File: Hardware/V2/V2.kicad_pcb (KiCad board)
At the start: 2 copper layers, 115 x 61 mm, 77 parts, among them J1 USB_B_Mini, Q1 MMBT2222, SW2 SW_Push, SW3 SW_Push, U1 ATmega32U4-AU, U2 LIS3DH, U4 AP2112K-3.3, Y1 16MHz

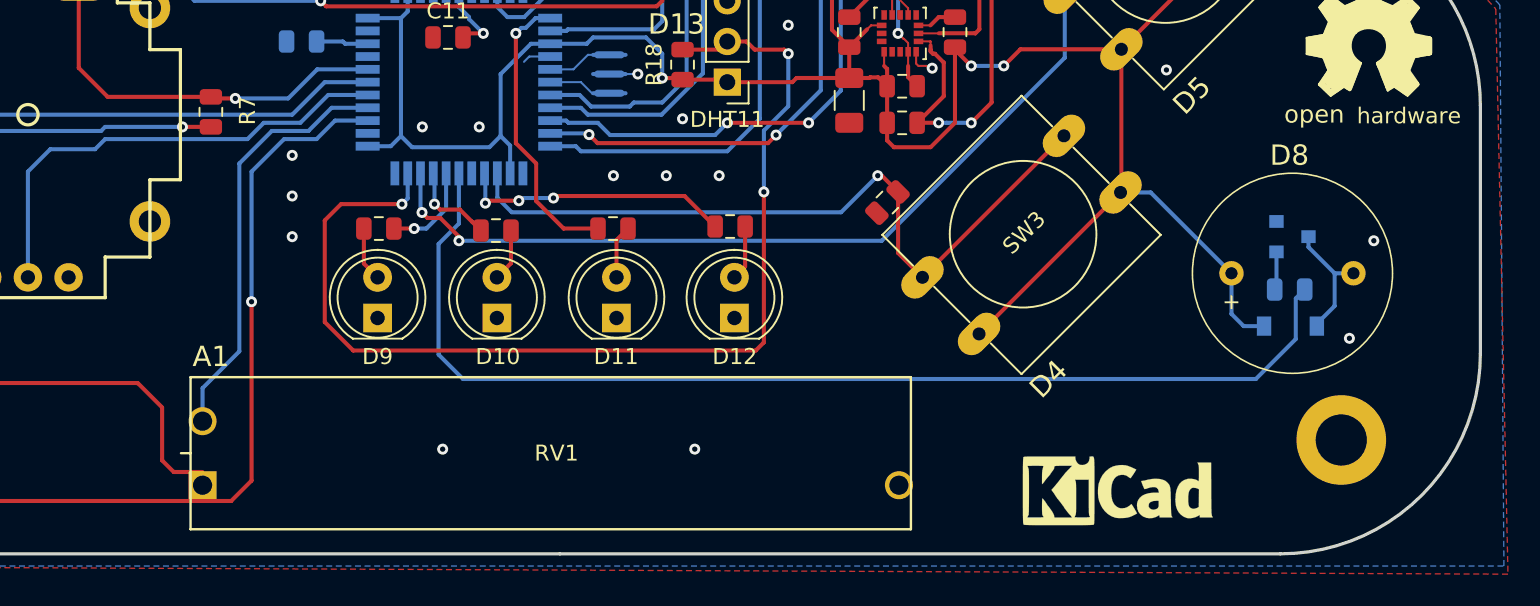
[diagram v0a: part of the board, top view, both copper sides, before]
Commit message: Serigrafias añadidas
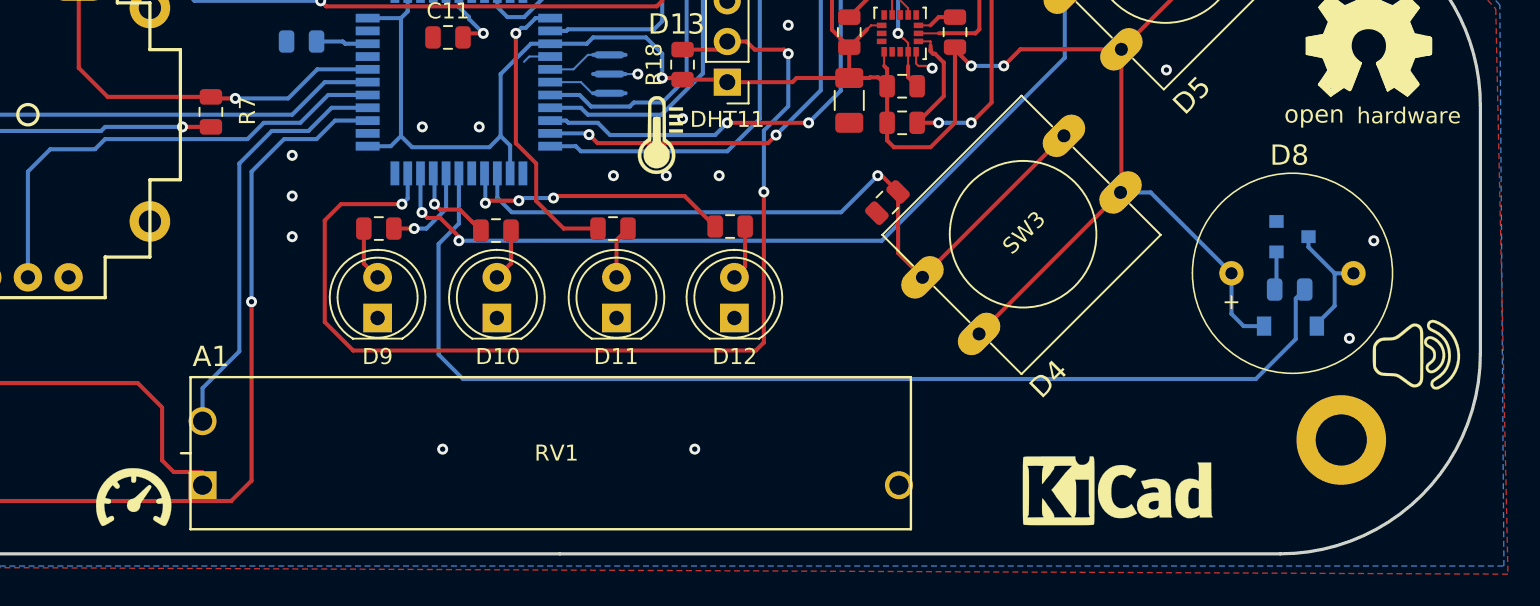
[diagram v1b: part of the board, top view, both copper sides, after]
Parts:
- added G***: LOGO, logos:altavoz, F.Cu at (209.9, 103.9)
- added G***: LOGO, logos:usb, B.Cu at (157.9, 66.9)
- added G***: LOGO, logos:bateria, B.Cu at (137.7, 61.3)
- added G***: LOGO, logos:cerebro, B.Cu at (140.1, 88.0)
- added G***: LOGO, logos:bt, B.Cu at (176.4, 76.5)
- added G***: LOGO, logos:pote, F.Cu at (129.8, 112.8)
- added G***: LOGO, logos:temp, F.Cu at (162.7, 90.2)

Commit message: DRC pasado
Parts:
- moved OLED_I2C 2.54 mm to (152.5, 71.1)
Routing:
- net GND: track 58.0 -> 60.6 mm, vias 44 -> 43
- net SDA: track 72.8 -> 74.5 mm, vias 3 -> 4
- net +3V3: track 395.9 -> 394.8 mm
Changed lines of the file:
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@@
     (thickness 1.6)
     (drawings 66)
-    (tracks 726)
+    (tracks 733)
     (zones 0)
     (modules 84)
@@
   (page A4)
   (layers
-    (0 F.Cu signal hide)
-    (31 B.Cu signal hide)
+    (0 F.Cu signal)
+    (31 B.Cu signal)
     (32 B.Adhes user)
     (33 F.Adhes user)
@@
   )
   (module Connector_PinHeader_2.54mm:PinHeader_1x04_P2.54mm_Vertical (layer F.Cu)
-    (at 152.4 73.66 90)
+    (at 152.527 71.12 90)
     (descr "Through hole straight pin header, 1x04, 2.54mm pitch, single row")
     (tags "Through hole pin header THT 1x04 2.54mm single row")
@@
   (gr_line (start 168.91 95.25) (end 142.24 95.25) (layer Dwgs.User) (width 0.127))
   (gr_line (start 168.91 67.31) (end 168.91 92.71) (layer Dwgs.User) (width 0.127))
-  (gr_line (start 142.24 67.31) (end 168.91 67.31) (layer Dwgs.User) (width 0.127))
+  (gr_line (start 142.24 69.088) (end 168.91 69.088) (layer Dwgs.User) (width 0.127))
   (segment (start 131.904 61.9) (end 133.352 60.452) (width 0.254) (layer F.Cu) (net 1))
   (segment (start 138.27 61.9) (end 138.52 61.9) (width 0.254) (layer F.Cu) (net 1) (status 30))
@@
   (segment (start 112.522 99.06) (end 120.65 99.06) (width 0.254) (layer B.Cu) (net 1) (status 20))
   (segment (start 110.998 97.536) (end 112.522 99.06) (width 0.254) (layer B.Cu) (net 1))
-  (segment (start 155.351 73.249) (end 154.94 73.66) (width 0.254) (layer F.Cu) (net 1) (status 30))
-  (segment (start 155.351 67.31) (end 155.351 73.249) (width 0.254) (layer F.Cu) (net 1) (status 30))
   (segment (start 139.954001 71.119999) (end 139.446 71.628) (width 0.254) (layer F.Cu) (net 1))
   (segment (start 139.954001 67.31) (end 139.954001 71.119999) (width 0.254) (layer F.Cu) (net 1) (status 10))
@@
   (segment (start 163.986999 86.614) (end 164.084 86.711001) (width 0.254) (layer F.Cu) (net 1) (status 30))
   (segment (start 162.814 86.614) (end 163.986999 86.614) (width 0.254) (layer F.Cu) (net 1) (status 20))
-  (segment (start 157.734 76.962) (end 157.734 77.47) (width 0.254) (layer F.Cu) (net 1) (status 30))
-  (segment (start 154.94 74.168) (end 157.734 76.962) (width 0.254) (layer F.Cu) (net 1) (status 30))
-  (segment (start 154.94 73.66) (end 154.94 74.168) (width 0.254) (layer F.Cu) (net 1) (status 30))
   (segment (start 152.02 90.932) (end 152.718 90.234) (width 0.254) (layer B.Cu) (net 1))
   (segment (start 147.192 90.932) (end 152.02 90.932) (width 0.254) (layer B.Cu) (net 1))
@@
   (segment (start 139.7 71.882) (end 139.446 71.628) (width 0.254) (layer F.Cu) (net 1))
   (segment (start 140.97 71.882) (end 139.7 71.882) (width 0.254) (layer F.Cu) (net 1))
-  (segment (start 163.068 67.056001) (end 162.814001 67.31) (width 0.254) (layer F.Cu) (net 1) (status 30))
-  (segment (start 161.38 61.9) (end 162.384 61.9) (width 0.254) (layer F.Cu) (net 1) (status 10))
-  (segment (start 163.068 65.786) (end 163.068 67.056001) (width 0.254) (layer F.Cu) (net 1) (status 20))
-  (segment (start 163.322 65.532) (end 163.068 65.786) (width 0.254) (layer F.Cu) (net 1))
-  (segment (start 162.384 61.9) (end 163.322 62.838) (width 0.254) (layer F.Cu) (net 1))
-  (segment (start 163.322 62.838) (end 163.322 65.532) (width 0.254) (layer F.Cu) (net 1))
   (segment (start 146.914 80.164) (end 146.914 81.168) (width 0.254) (layer B.Cu) (net 1) (status 20))
   (segment (start 146.812 80.062) (end 146.914 80.164) (width 0.254) (layer B.Cu) (net 1))
@@
   (segment (start 170.591 68.6735) (end 172.6565 70.739) (width 0.254) (layer F.Cu) (net 1) (status 20))
   (segment (start 170.591 67.31) (end 170.591 68.6735) (width 0.254) (layer F.Cu) (net 1) (status 10))
+  (segment (start 157.734 76.962) (end 157.734 77.47) (width 0.254) (layer F.Cu) (net 1))
+  (segment (start 155.351 74.579) (end 157.734 76.962) (width 0.254) (layer F.Cu) (net 1))
+  (segment (start 155.351 72.606081) (end 155.351 74.579) (width 0.254) (layer F.Cu) (net 1))
+  (segment (start 155.067 72.322081) (end 155.351 72.606081) (width 0.254) (layer F.Cu) (net 1))
+  (segment (start 155.067 71.12) (end 155.067 72.322081) (width 0.254) (layer F.Cu) (net 1))
+  (segment (start 154.26999 68.39101) (end 154.37001 68.39101) (width 0.254) (layer F.Cu) (net 1))
+  (segment (start 155.067 69.088) (end 155.067 71.12) (width 0.254) (layer F.Cu) (net 1))
+  (segment (start 154.37001 68.39101) (end 155.067 69.088) (width 0.254) (layer F.Cu) (net 1))
+  (segment (start 163.068 67.056001) (end 162.814001 67.31) (width 0.254) (layer F.Cu) (net 1))
+  (segment (start 163.068 65.786) (end 163.068 67.056001) (width 0.254) (layer F.Cu) (net 1))
+  (segment (start 162.941 65.659) (end 163.068 65.786) (width 0.254) (layer F.Cu) (net 1))
+  (segment (start 162.941 62.457) (end 162.941 65.659) (width 0.254) (layer F.Cu) (net 1))
+  (segment (start 162.384 61.9) (end 162.941 62.457) (width 0.254) (layer F.Cu) (net 1))
+  (segment (start 161.38 61.9) (end 162.384 61.9) (width 0.254) (layer F.Cu) (net 1))
   (segment (start 204.816 98.806) (end 205.994 98.806) (width 0.254) (layer B.Cu) (net 2) (status 20))
   (segment (start 203.184 97.174) (end 204.816 98.806) (width 0.254) (layer B.Cu) (net 2))
@@
   (segment (start 152.146 78.486) (end 152.146 79.248) (width 0.254) (layer B.Cu) (net 3))
   (segment (start 153.416 77.216) (end 152.146 78.486) (width 0.254) (layer B.Cu) (net 3) (status 10))
-  (segment (start 152.4 76.297) (end 152.4 73.66) (width 0.254) (layer B.Cu) (net 3) (status 20))
-  (segment (start 151.481 77.216) (end 152.4 76.297) (width 0.254) (layer B.Cu) (net 3) (status 10))
   (segment (start 141.964 67.31) (end 141.829001 67.31) (width 0.254) (layer F.Cu) (net 3) (status 30))
   (segment (start 143.42 65.854) (end 141.964 67.31) (width 0.254) (layer F.Cu) (net 3) (status 20))
@@
   (via (at 170.688 76.708) (size 0.6858) (drill 0.3302) (layers F.Cu B.Cu) (net 3))
   (via (at 163.83 70.866) (size 0.6858) (drill 0.3302) (layers F.Cu B.Cu) (net 3))
-  (via (at 160.02 70.866) (size 0.6858) (drill 0.3302) (layers F.Cu B.Cu) (net 3))
   (via (at 154.94 57.404) (size 0.6858) (drill 0.3302) (layers F.Cu B.Cu) (net 3))
   (via (at 156.21 57.404) (size 0.6858) (drill 0.3302) (layers F.Cu B.Cu) (net 3))
@@
   (via (at 139.7 93.98) (size 0.6858) (drill 0.3302) (layers F.Cu B.Cu) (net 3))
   (via (at 139.7 96.52) (size 0.6858) (drill 0.3302) (layers F.Cu B.Cu) (net 3))
+  (segment (start 152.527 73.533) (end 152.527 71.12) (width 0.254) (layer B.Cu) (net 3))
+  (segment (start 152.527 76.17) (end 152.527 73.533) (width 0.254) (layer B.Cu) (net 3))
+  (segment (start 151.481 77.216) (end 152.527 76.17) (width 0.254) (layer B.Cu) (net 3))
   (segment (start 149.606 78.486) (end 149.606 77.216) (width 0.254) (layer B.Cu) (net 4) (status 20))
   (segment (start 150.914 79.794) (end 149.606 78.486) (width 0.254) (layer B.Cu) (net 4))
@@
   (segment (start 178.172999 85.852) (end 178.172999 86.557499) (width 0.254) (layer F.Cu) (net 25))
   (segment (start 178.172999 84.97) (end 178.172999 85.852) (width 0.127) (layer F.Cu) (net 25) (status 10))
-  (segment (start 157.48 73.66) (end 159.258 71.882) (width 0.254) (layer F.Cu) (net 25) (status 10))
-  (segment (start 159.258 71.882) (end 161.29 71.882) (width 0.254) (layer F.Cu) (net 25))
-  (segment (start 161.29 71.882) (end 162.306 72.898) (width 0.254) (layer F.Cu) (net 25))
   (via (at 177.546 72.898) (size 0.6858) (drill 0.3302) (layers F.Cu B.Cu) (net 25))
   (segment (start 162.306 72.898) (end 177.546 72.898) (width 0.254) (layer F.Cu) (net 25))
@@
   (segment (start 161.036011 88.137989) (end 162.814009 88.137989) (width 0.254) (layer B.Cu) (net 25))
   (segment (start 155.814 87.668) (end 157.651368 87.668) (width 0.254) (layer B.Cu) (net 25) (status 10))
+  (segment (start 158.182919 72.898) (end 162.306 72.898) (width 0.254) (layer F.Cu) (net 25))
+  (segment (start 157.607 72.322081) (end 158.182919 72.898) (width 0.254) (layer F.Cu) (net 25))
+  (segment (start 157.607 71.12) (end 157.607 72.322081) (width 0.254) (layer F.Cu) (net 25))
   (segment (start 154.643 81.168) (end 155.801 80.01) (width 0.254) (layer B.Cu) (net 26))
   (segment (start 154.114 81.168) (end 154.643 81.168) (width 0.254) (layer B.Cu) (net 26) (status 10))
@@
   (via (at 165.354 74.93) (size 0.6858) (drill 0.3302) (layers F.Cu B.Cu) (net 63))
   (segment (start 165.354 74.93) (end 165.354 73.66) (width 0.254) (layer F.Cu) (net 63))
-  (segment (start 160.02 73.66) (end 165.354 73.66) (width 0.254) (layer F.Cu) (net 63) (status 10))
   (segment (start 183.388 88.138) (end 182.118 89.408) (width 0.254) (layer F.Cu) (net 63))
   (segment (start 183.388 75.184) (end 183.388 88.138) (width 0.254) (layer F.Cu) (net 63))
@@
   (segment (start 155.814 88.468) (end 157.732934 88.468) (width 0.254) (layer B.Cu) (net 63) (status 10))
   (segment (start 162.770434 88.9) (end 165.354 86.316434) (width 0.254) (layer B.Cu) (net 63))
+  (via (at 161.29 73.66) (size 0.6858) (drill 0.3302) (layers F.Cu B.Cu) (net 63))
+  (segment (start 160.147 72.517) (end 160.947101 73.317101) (width 0.254) (layer B.Cu) (net 63))
+  (segment (start 165.354 73.66) (end 161.29 73.66) (width 0.254) (layer F.Cu) (net 63))
+  (segment (start 160.147 71.12) (end 160.147 72.517) (width 0.254) (layer B.Cu) (net 63))
+  (segment (start 160.947101 73.317101) (end 161.29 73.66) (width 0.254) (layer B.Cu) (net 63))
   (segment (start 155.814 86.068) (end 157.264 86.068) (width 0.127) (layer B.Cu) (net 64) (status 10))
   (segment (start 158.17088 85.16112) (end 159.512 85.16112) (width 0.127) (layer B.Cu) (net 64) (status 20))

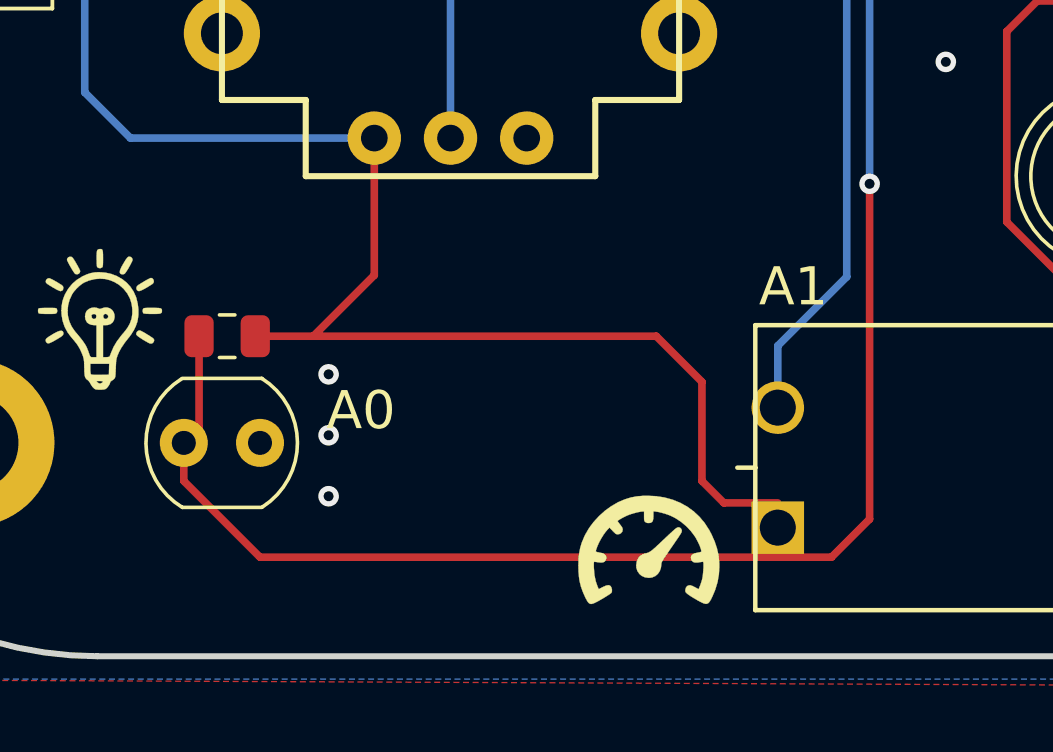
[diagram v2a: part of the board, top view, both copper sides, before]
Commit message: Taladros del Slider ensanchados
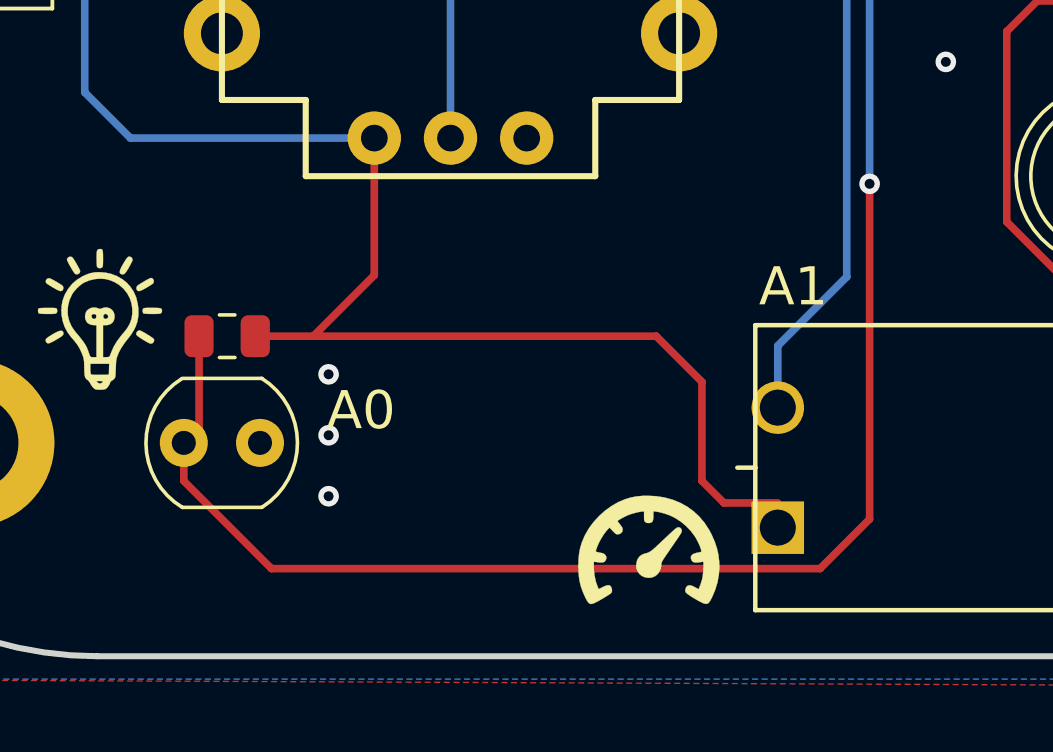
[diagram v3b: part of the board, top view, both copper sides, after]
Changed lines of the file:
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@@
   (general
     (thickness 1.6)
-    (drawings 66)
+    (drawings 67)
     (tracks 733)
     (zones 0)
@@
     (visible_elements FFFFFF7F)
     (pcbplotparams
-      (layerselection 0x31000_7ffffffe)
+      (layerselection 0x31003_7ffffffe)
       (usegerberextensions true)
       (usegerberattributes true)
@@
       (psnegative false)
       (psa4output false)
-      (plotreference true)
-      (plotvalue true)
+      (plotreference false)
+      (plotvalue false)
       (plotinvisibletext false)
       (padsonsilk false)
@@
       (xy -0.194733 -2.429588)) (layer F.SilkS) (width 0.01))
   )
+  (dimension 114.935 (width 0.127) (layer F.SilkS)
+    (gr_text "114.935 mm" (at 156.4005 139.03) (layer F.SilkS)
+      (effects (font (size 0.6 0.6) (thickness 0.127)))
+    )
+    (feature1 (pts (xy 98.933 98.806) (xy 98.933 138.762421)))
+    (feature2 (pts (xy 213.868 98.806) (xy 213.868 138.762421)))
+    (crossbar (pts (xy 213.868 138.176) (xy 98.933 138.176)))
+    (arrow1a (pts (xy 98.933 138.176) (xy 100.059504 137.589579)))
+    (arrow1b (pts (xy 98.933 138.176) (xy 100.059504 138.762421)))
+    (arrow2a (pts (xy 213.868 138.176) (xy 212.741496 137.589579)))
+    (arrow2b (pts (xy 213.868 138.176) (xy 212.741496 138.762421)))
+  )
   (gr_text z (at 174.879 75.184) (layer F.SilkS)
     (effects (font (size 0.6 0.6) (thickness 0.127)))
@@
   (segment (start 114.808 105.664) (end 114.808 108.712) (width 0.254) (layer F.Cu) (net 37) (status 30))
   (via (at 137.16 100.584) (size 0.6858) (drill 0.3302) (layers F.Cu B.Cu) (net 37))
-  (segment (start 114.3 110.49) (end 114.3 109.22) (width 0.254) (layer F.Cu) (net 37) (status 20))
-  (segment (start 116.84 113.03) (end 114.3 110.49) (width 0.254) (layer F.Cu) (net 37))
-  (segment (start 137.16 111.76) (end 135.89 113.03) (width 0.254) (layer F.Cu) (net 37))
-  (segment (start 137.16 100.584) (end 137.16 111.76) (width 0.254) (layer F.Cu) (net 37))
   (segment (start 137.16 92.456) (end 137.16 100.584) (width 0.254) (layer B.Cu) (net 37))
   (segment (start 139.192 90.424) (end 137.16 92.456) (width 0.254) (layer B.Cu) (net 37))
@@
   (segment (start 142.38 89.268) (end 141.224 90.424) (width 0.254) (layer B.Cu) (net 37))
   (segment (start 144.414 89.268) (end 142.38 89.268) (width 0.254) (layer B.Cu) (net 37) (status 10))
-  (segment (start 116.84 113.03) (end 135.89 113.03) (width 0.254) (layer F.Cu) (net 37))
+  (segment (start 137.16 111.76) (end 137.16 100.584) (width 0.254) (layer F.Cu) (net 37))
+  (segment (start 135.509 113.411) (end 137.16 111.76) (width 0.254) (layer F.Cu) (net 37))
+  (segment (start 114.3 110.49) (end 117.221 113.411) (width 0.254) (layer F.Cu) (net 37))
+  (segment (start 117.221 113.411) (end 135.509 113.411) (width 0.254) (layer F.Cu) (net 37))
+  (segment (start 114.3 109.22) (end 114.3 110.49) (width 0.254) (layer F.Cu) (net 37))
   (segment (start 184.912 78.232) (end 187.96 81.28) (width 0.254) (layer F.Cu) (net 38) (status 20))
   (segment (start 184.912 77.216) (end 184.912 78.232) (width 0.254) (layer F.Cu) (net 38) (status 10))
